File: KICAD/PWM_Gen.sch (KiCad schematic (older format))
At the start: 13 parts, among them U1 AD8030, U2 AD8030

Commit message: review w/ jmt
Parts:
- C26: renamed from C?; footprint Capacitor_SMD:C_0805_2012Metric_Pad1.15x1.40mm_HandSolder -> (none)
- R70, R71, R72, R73, R74, R75: renamed from R?; footprint Resistor_SMD:R_0805_2012Metric_Pad1.15x1.40mm_HandSolder -> (none)
- U1: footprint Package_SO:SO-8_3.9x4.9mm_P1.27mm -> (none)
- U13: renamed from U2; footprint Package_SO:SO-8_3.9x4.9mm_P1.27mm -> (none)
- gave numbers to parts that had none: 4
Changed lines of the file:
@@
 $Descr A4 11693 8268
 encoding utf-8
-Sheet 14 17
+Sheet 13 17
 Title "SESAME"
 Date ""
@@
 AR Path="/60F19D5B/613D641B" Ref="R?"  Part="1"
 AR Path="/60F171CE/613D641B" Ref="R?"  Part="1"
-AR Path="/60F1AF26/613D641B" Ref="R?"  Part="1"
-F 0 "R?" V 5207 3050 50  0000 C CNN
+AR Path="/60F1AF26/613D641B" Ref="R73"  Part="1"
+F 0 "R73" V 5207 3050 50  0000 C CNN
 F 1 "100k" V 5116 3050 50  0000 C CNN
-F 2 "Resistor_SMD:R_0805_2012Metric_Pad1.15x1.40mm_HandSolder" V 4930 3050 50  0001 C CNN
+F 2 "" V 4930 3050 50  0001 C CNN
 F 3 "~" H 5000 3050 50  0001 C CNN
 	1    5000 3050
@@
 AR Path="/60F19D5B/613D6415" Ref="R?"  Part="1"
 AR Path="/60F171CE/613D6415" Ref="R?"  Part="1"
-AR Path="/60F1AF26/613D6415" Ref="R?"  Part="1"
-F 0 "R?" V 5207 2850 50  0000 C CNN
+AR Path="/60F1AF26/613D6415" Ref="R72"  Part="1"
+F 0 "R72" V 5207 2850 50  0000 C CNN
 F 1 "100k" V 5116 2850 50  0000 C CNN
-F 2 "Resistor_SMD:R_0805_2012Metric_Pad1.15x1.40mm_HandSolder" V 4930 2850 50  0001 C CNN
+F 2 "" V 4930 2850 50  0001 C CNN
 F 3 "~" H 5000 2850 50  0001 C CNN
 	1    5000 2850
@@
 AR Path="/60F19D5B/613D6432" Ref="#PWR?"  Part="1"
 AR Path="/60F171CE/613D6432" Ref="#PWR?"  Part="1"
-AR Path="/60F1AF26/613D6432" Ref="#PWR0116"  Part="1"
-F 0 "#PWR0116" H 5350 3300 50  0001 C CNN
+AR Path="/60F1AF26/613D6432" Ref="#PWR090"  Part="1"
+F 0 "#PWR090" H 5350 3300 50  0001 C CNN
 F 1 "GND" H 5355 3377 50  0000 C CNN
 F 2 "" H 5350 3550 50  0001 C CNN
@@
 AR Path="/60F19D5B/613D6429" Ref="R?"  Part="1"
 AR Path="/60F171CE/613D6429" Ref="R?"  Part="1"
-AR Path="/60F1AF26/613D6429" Ref="R?"  Part="1"
-F 0 "R?" H 5420 3446 50  0000 L CNN
+AR Path="/60F1AF26/613D6429" Ref="R74"  Part="1"
+F 0 "R74" H 5420 3446 50  0000 L CNN
 F 1 "100k" H 5420 3355 50  0000 L CNN
-F 2 "Resistor_SMD:R_0805_2012Metric_Pad1.15x1.40mm_HandSolder" V 5280 3400 50  0001 C CNN
+F 2 "" V 5280 3400 50  0001 C CNN
 F 3 "~" H 5350 3400 50  0001 C CNN
 	1    5350 3400
@@
 AR Path="/60F19D5B/613D9855" Ref="R?"  Part="1"
 AR Path="/60F171CE/613D9855" Ref="R?"  Part="1"
-AR Path="/60F1AF26/613D9855" Ref="R?"  Part="1"
-F 0 "R?" H 3070 3096 50  0000 L CNN
+AR Path="/60F1AF26/613D9855" Ref="R71"  Part="1"
+F 0 "R71" H 3070 3096 50  0000 L CNN
 F 1 "4.7k" H 3070 3005 50  0000 L CNN
-F 2 "Resistor_SMD:R_0805_2012Metric_Pad1.15x1.40mm_HandSolder" V 2930 3050 50  0001 C CNN
+F 2 "" V 2930 3050 50  0001 C CNN
 F 3 "~" H 3000 3050 50  0001 C CNN
 	1    3000 3050
@@
 AR Path="/60F19D5B/613D9F4F" Ref="#PWR?"  Part="1"
 AR Path="/60F171CE/613D9F4F" Ref="#PWR?"  Part="1"
-AR Path="/60F1AF26/613D9F4F" Ref="#PWR0117"  Part="1"
-F 0 "#PWR0117" H 3000 2950 50  0001 C CNN
+AR Path="/60F1AF26/613D9F4F" Ref="#PWR089"  Part="1"
+F 0 "#PWR089" H 3000 2950 50  0001 C CNN
 F 1 "GND" H 3005 3027 50  0000 C CNN
 F 2 "" H 3000 3200 50  0001 C CNN
@@
 Same IC package than the Feedback block
 $Comp
-L Sesame:AD8030 U2
+L Sesame:AD8030 U13
 U 1 1 6128401D
 P 8200 3050
-F 0 "U2" H 8200 2683 50  0000 C CNN
+F 0 "U13" H 8200 2683 50  0000 C CNN
 F 1 "AD8030" H 8200 2774 50  0000 C CNN
-F 2 "Package_SO:SO-8_3.9x4.9mm_P1.27mm" H 8200 3050 50  0001 C CNN
+F 2 "" H 8200 3050 50  0001 C CNN
 F 3 "~" H 8200 3050 50  0001 C CNN
 	1    8200 3050
@@
 $EndComp
 $Comp
-L Sesame:AD8030 U2
+L Sesame:AD8030 U13
 U 2 1 61284FE7
 P 8200 3950
-F 0 "U2" H 8200 3583 50  0000 C CNN
+F 0 "U13" H 8200 3583 50  0000 C CNN
 F 1 "AD8030" H 8200 3674 50  0000 C CNN
-F 2 "Package_SO:SO-8_3.9x4.9mm_P1.27mm" H 8200 3950 50  0001 C CNN
+F 2 "" H 8200 3950 50  0001 C CNN
 F 3 "~" H 8200 3950 50  0001 C CNN
 	2    8200 3950
@@
 F 0 "U1" H 5700 3350 50  0000 C CNN
 F 1 "AD8030" H 5700 3250 50  0000 C CNN
-F 2 "Package_SO:SO-8_3.9x4.9mm_P1.27mm" H 5700 2950 50  0001 C CNN
+F 2 "" H 5700 2950 50  0001 C CNN
 F 3 "~" H 5700 2950 50  0001 C CNN
 	2    5700 2950
@@
 $EndComp
 $Comp
-L Sesame:VREF #PWR0120
+L Sesame:VREF #PWR088
 U 1 1 6154E004
 P 3000 2500
-F 0 "#PWR0120" H 3000 2350 50  0001 C CNN
+F 0 "#PWR088" H 3000 2350 50  0001 C CNN
 F 1 "VREF" H 3015 2673 50  0000 C CNN
 F 2 "" H 3000 2500 50  0001 C CNN
@@
 AR Path="/60F19D5B/613D8CB8" Ref="R?"  Part="1"
 AR Path="/60F171CE/613D8CB8" Ref="R?"  Part="1"
-AR Path="/60F1AF26/613D8CB8" Ref="R?"  Part="1"
-F 0 "R?" H 3070 2696 50  0000 L CNN
+AR Path="/60F1AF26/613D8CB8" Ref="R70"  Part="1"
+F 0 "R70" H 3070 2696 50  0000 L CNN
 F 1 "100k" H 3070 2605 50  0000 L CNN
-F 2 "Resistor_SMD:R_0805_2012Metric_Pad1.15x1.40mm_HandSolder" V 2930 2650 50  0001 C CNN
+F 2 "" V 2930 2650 50  0001 C CNN
 F 3 "~" H 3000 2650 50  0001 C CNN
 	1    3000 2650
@@
 $EndComp
 $Comp
-L Connector:TestPoint TP?
+L Connector:TestPoint TP35
 U 1 1 612937F6
 P 3900 2850
-F 0 "TP?" H 3850 3100 50  0000 L CNN
+F 0 "TP35" H 3850 3100 50  0000 L CNN
 F 1 "TP_NOP" H 3900 2750 50  0000 C CNN
 F 2 "" H 4100 2850 50  0001 C CNN
@@
 	3000 2850 3900 2850
 $Comp
-L Connector:TestPoint TP?
+L Connector:TestPoint TP36
 U 1 1 61299A59
 P 6600 2950
-F 0 "TP?" H 6550 3200 50  0000 L CNN
+F 0 "TP36" H 6550 3200 50  0000 L CNN
 F 1 "TP_POP" H 6600 2850 50  0000 C CNN
 F 2 "" H 6800 2950 50  0001 C CNN
@@
 	6600 2950 7900 2950
 $Comp
-L Connector:TestPoint TP?
+L Connector:TestPoint TP38
 U 1 1 612A9FCA
 P 9150 3950
-F 0 "TP?" H 9100 4200 50  0000 L CNN
+F 0 "TP38" H 9100 4200 50  0000 L CNN
 F 1 "TP_POP" H 9150 3850 50  0000 C CNN
 F 2 "" H 9350 3950 50  0001 C CNN
@@
 	9150 3950 8500 3950
 $Comp
-L Connector:TestPoint TP?
+L Connector:TestPoint TP37
 U 1 1 612A923F
 P 9150 3050
-F 0 "TP?" H 9100 3300 50  0000 L CNN
+F 0 "TP37" H 9100 3300 50  0000 L CNN
 F 1 "TP_POP" H 9150 2950 50  0000 C CNN
 F 2 "" H 9350 3050 50  0001 C CNN
@@
 OP Amp supply
 $Comp
-L Device:C C?
+L Device:C C26
 U 1 1 612CB355
 P 1350 6900
-AR Path="/60F1AF26/612CB355" Ref="C?"  Part="1"
+AR Path="/60F1AF26/612CB355" Ref="C26"  Part="1"
 AR Path="/60F1B237/612CB355" Ref="C?"  Part="1"
-F 0 "C?" H 1465 6946 50  0000 L CNN
+F 0 "C26" H 1465 6946 50  0000 L CNN
 F 1 "100n" H 1465 6855 50  0000 L CNN
-F 2 "Capacitor_SMD:C_0805_2012Metric_Pad1.15x1.40mm_HandSolder" H 1388 6750 50  0001 C CNN
+F 2 "" H 1388 6750 50  0001 C CNN
 F 3 "~" H 1350 6900 50  0001 C CNN
 	1    1350 6900
@@
 	1050 7250 1050 7200
 $Comp
-L power:GND #PWR?
+L power:GND #PWR087
 U 1 1 612CB360
 P 1200 7300
-AR Path="/60F1AF26/612CB360" Ref="#PWR?"  Part="1"
+AR Path="/60F1AF26/612CB360" Ref="#PWR087"  Part="1"
 AR Path="/60F1B237/612CB360" Ref="#PWR?"  Part="1"
-F 0 "#PWR?" H 1200 7050 50  0001 C CNN
+F 0 "#PWR087" H 1200 7050 50  0001 C CNN
 F 1 "GND" H 1205 7127 50  0000 C CNN
 F 2 "" H 1200 7300 50  0001 C CNN
@@
 	1200 7250 1350 7250
 $Comp
-L power:VCC #PWR?
+L power:VCC #PWR086
 U 1 1 612CB36D
 P 1200 6500
-AR Path="/60F1AF26/612CB36D" Ref="#PWR?"  Part="1"
+AR Path="/60F1AF26/612CB36D" Ref="#PWR086"  Part="1"
 AR Path="/60F1B237/612CB36D" Ref="#PWR?"  Part="1"
-F 0 "#PWR?" H 1200 6350 50  0001 C CNN
+F 0 "#PWR086" H 1200 6350 50  0001 C CNN
 F 1 "VCC" H 1215 6673 50  0000 C CNN
 F 2 "" H 1200 6500 50  0001 C CNN
@@
 $EndComp
 $Comp
-L Sesame:AD8030 U2
+L Sesame:AD8030 U13
 U 3 1 612CB373
 P 1150 6900
-AR Path="/60F1AF26/612CB373" Ref="U2"  Part="3"
+AR Path="/60F1AF26/612CB373" Ref="U13"  Part="3"
 AR Path="/60F1B237/612CB373" Ref="U?"  Part="3"
-F 0 "U2" H 963 6854 50  0000 R CNN
+F 0 "U13" H 963 6854 50  0000 R CNN
 F 1 "AD8030" H 963 6945 50  0000 R CNN
-F 2 "Package_SO:SO-8_3.9x4.9mm_P1.27mm" H 1150 6900 50  0001 C CNN
+F 2 "" H 1150 6900 50  0001 C CNN
 F 3 "~" H 1150 6900 50  0001 C CNN
 	3    1150 6900
@@
 AR Path="/60F19D5B/613D640F" Ref="R?"  Part="1"
 AR Path="/60F171CE/613D640F" Ref="R?"  Part="1"
-AR Path="/60F1AF26/613D640F" Ref="R?"  Part="1"
-F 0 "R?" V 5907 2600 50  0000 C CNN
+AR Path="/60F1AF26/613D640F" Ref="R75"  Part="1"
+F 0 "R75" V 5907 2600 50  0000 C CNN
 F 1 "100k" V 5816 2600 50  0000 C CNN
-F 2 "Resistor_SMD:R_0805_2012Metric_Pad1.15x1.40mm_HandSolder" V 5630 2600 50  0001 C CNN
+F 2 "" V 5630 2600 50  0001 C CNN
 F 3 "~" H 5700 2600 50  0001 C CNN
 	1    5700 2600

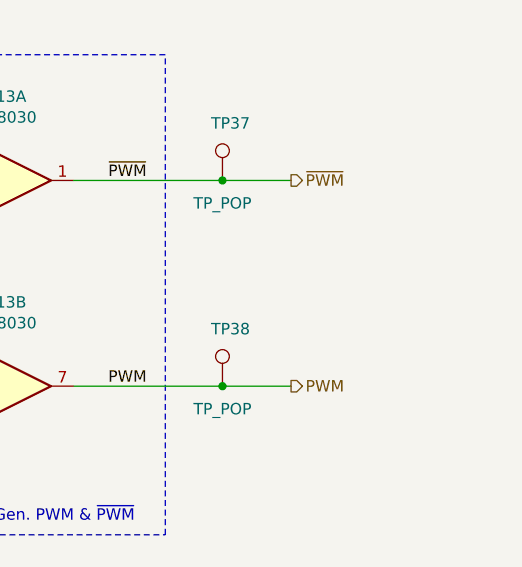
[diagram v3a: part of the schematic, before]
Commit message: edit footprints by jmt
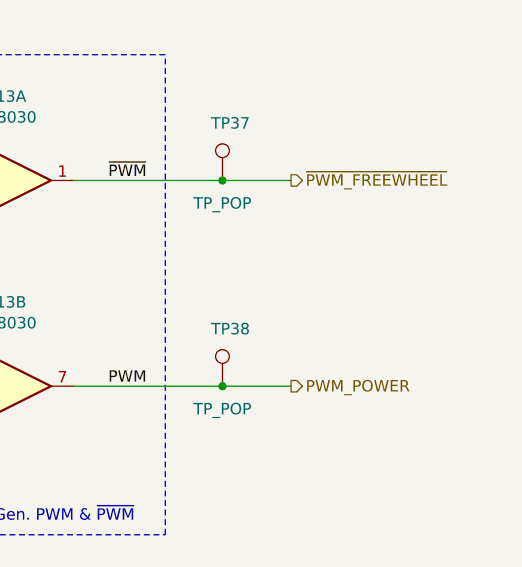
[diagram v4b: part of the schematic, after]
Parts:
- C26: footprint (none) -> Capacitor_SMD:C_0805_2012Metric_Pad1.15x1.40mm_HandSolder
- R70, R71, R72, R73, R74, R75: footprint (none) -> Resistor_SMD:R_0805_2012Metric_Pad1.15x1.40mm_HandSolder
- TP35: footprint (none) -> TestPoint:TestPoint_THTPad_D2.0mm_Drill1.0mm
- TP36, TP37, TP38: footprint (none) -> TestPoint:TestPoint_Loop_D1.80mm_Drill1.0mm_Beaded
- U1, U13: footprint (none) -> Package_SO:SO-8_5.3x6.2mm_P1.27mm
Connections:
- net PWM renamed PWM_POWER
- net ~PWM renamed ~PWM_FREEWHEEL
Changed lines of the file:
@@
 F 0 "R73" V 5207 3050 50  0000 C CNN
 F 1 "100k" V 5116 3050 50  0000 C CNN
-F 2 "" V 4930 3050 50  0001 C CNN
+F 2 "Resistor_SMD:R_0805_2012Metric_Pad1.15x1.40mm_HandSolder" V 4930 3050 50  0001 C CNN
 F 3 "~" H 5000 3050 50  0001 C CNN
 	1    5000 3050
@@
 F 0 "R72" V 5207 2850 50  0000 C CNN
 F 1 "100k" V 5116 2850 50  0000 C CNN
-F 2 "" V 4930 2850 50  0001 C CNN
+F 2 "Resistor_SMD:R_0805_2012Metric_Pad1.15x1.40mm_HandSolder" V 4930 2850 50  0001 C CNN
 F 3 "~" H 5000 2850 50  0001 C CNN
 	1    5000 2850
@@
 F 0 "R74" H 5420 3446 50  0000 L CNN
 F 1 "100k" H 5420 3355 50  0000 L CNN
-F 2 "" V 5280 3400 50  0001 C CNN
+F 2 "Resistor_SMD:R_0805_2012Metric_Pad1.15x1.40mm_HandSolder" V 5280 3400 50  0001 C CNN
 F 3 "~" H 5350 3400 50  0001 C CNN
 	1    5350 3400
@@
 F 0 "R71" H 3070 3096 50  0000 L CNN
 F 1 "4.7k" H 3070 3005 50  0000 L CNN
-F 2 "" V 2930 3050 50  0001 C CNN
+F 2 "Resistor_SMD:R_0805_2012Metric_Pad1.15x1.40mm_HandSolder" V 2930 3050 50  0001 C CNN
 F 3 "~" H 3000 3050 50  0001 C CNN
 	1    3000 3050
@@
 	8500 3050 9150 3050
 Text HLabel 9450 3050 2    50   Output ~ 0
-~PWM
+~PWM_FREEWHEEL
 Text HLabel 9450 3950 2    50   Output ~ 0
-PWM
+PWM_POWER
 Text HLabel 6850 3500 0    50   Input ~ 0
 Ramp
@@
 F 0 "U13" H 8200 2683 50  0000 C CNN
 F 1 "AD8030" H 8200 2774 50  0000 C CNN
-F 2 "" H 8200 3050 50  0001 C CNN
+F 2 "Package_SO:SO-8_5.3x6.2mm_P1.27mm" H 8200 3050 50  0001 C CNN
 F 3 "~" H 8200 3050 50  0001 C CNN
 	1    8200 3050
@@
 F 0 "U13" H 8200 3583 50  0000 C CNN
 F 1 "AD8030" H 8200 3674 50  0000 C CNN
-F 2 "" H 8200 3950 50  0001 C CNN
+F 2 "Package_SO:SO-8_5.3x6.2mm_P1.27mm" H 8200 3950 50  0001 C CNN
 F 3 "~" H 8200 3950 50  0001 C CNN
 	2    8200 3950
@@
 F 0 "U1" H 5700 3350 50  0000 C CNN
 F 1 "AD8030" H 5700 3250 50  0000 C CNN
-F 2 "" H 5700 2950 50  0001 C CNN
+F 2 "Package_SO:SO-8_5.3x6.2mm_P1.27mm" H 5700 2950 50  0001 C CNN
 F 3 "~" H 5700 2950 50  0001 C CNN
 	2    5700 2950
@@
 F 0 "R70" H 3070 2696 50  0000 L CNN
 F 1 "100k" H 3070 2605 50  0000 L CNN
-F 2 "" V 2930 2650 50  0001 C CNN
+F 2 "Resistor_SMD:R_0805_2012Metric_Pad1.15x1.40mm_HandSolder" V 2930 2650 50  0001 C CNN
 F 3 "~" H 3000 2650 50  0001 C CNN
 	1    3000 2650
@@
 F 0 "TP35" H 3850 3100 50  0000 L CNN
 F 1 "TP_NOP" H 3900 2750 50  0000 C CNN
-F 2 "" H 4100 2850 50  0001 C CNN
+F 2 "TestPoint:TestPoint_THTPad_D2.0mm_Drill1.0mm" H 4100 2850 50  0001 C CNN
 F 3 "~" H 4100 2850 50  0001 C CNN
 	1    3900 2850
@@
 F 0 "TP36" H 6550 3200 50  0000 L CNN
 F 1 "TP_POP" H 6600 2850 50  0000 C CNN
-F 2 "" H 6800 2950 50  0001 C CNN
+F 2 "TestPoint:TestPoint_Loop_D1.80mm_Drill1.0mm_Beaded" H 6800 2950 50  0001 C CNN
 F 3 "~" H 6800 2950 50  0001 C CNN
 	1    6600 2950
@@
 F 0 "TP38" H 9100 4200 50  0000 L CNN
 F 1 "TP_POP" H 9150 3850 50  0000 C CNN
-F 2 "" H 9350 3950 50  0001 C CNN
+F 2 "TestPoint:TestPoint_Loop_D1.80mm_Drill1.0mm_Beaded" H 9350 3950 50  0001 C CNN
 F 3 "~" H 9350 3950 50  0001 C CNN
 	1    9150 3950
@@
 F 0 "TP37" H 9100 3300 50  0000 L CNN
 F 1 "TP_POP" H 9150 2950 50  0000 C CNN
-F 2 "" H 9350 3050 50  0001 C CNN
+F 2 "TestPoint:TestPoint_Loop_D1.80mm_Drill1.0mm_Beaded" H 9350 3050 50  0001 C CNN
 F 3 "~" H 9350 3050 50  0001 C CNN
 	1    9150 3050
@@
 F 0 "C26" H 1465 6946 50  0000 L CNN
 F 1 "100n" H 1465 6855 50  0000 L CNN
-F 2 "" H 1388 6750 50  0001 C CNN
+F 2 "Capacitor_SMD:C_0805_2012Metric_Pad1.15x1.40mm_HandSolder" H 1388 6750 50  0001 C CNN
 F 3 "~" H 1350 6900 50  0001 C CNN
 	1    1350 6900
@@
 F 0 "U13" H 963 6854 50  0000 R CNN
 F 1 "AD8030" H 963 6945 50  0000 R CNN
-F 2 "" H 1150 6900 50  0001 C CNN
+F 2 "Package_SO:SO-8_5.3x6.2mm_P1.27mm" H 1150 6900 50  0001 C CNN
 F 3 "~" H 1150 6900 50  0001 C CNN
 	3    1150 6900
@@
 F 0 "R75" V 5907 2600 50  0000 C CNN
 F 1 "100k" V 5816 2600 50  0000 C CNN
-F 2 "" V 5630 2600 50  0001 C CNN
+F 2 "Resistor_SMD:R_0805_2012Metric_Pad1.15x1.40mm_HandSolder" V 5630 2600 50  0001 C CNN
 F 3 "~" H 5700 2600 50  0001 C CNN
 	1    5700 2600

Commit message: route + work on djd
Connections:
- net PWM_POWER renamed PWM_Power
- net ~PWM_FREEWHEEL renamed ~PWM_Freewheel
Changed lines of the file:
@@
 $Descr A4 11693 8268
 encoding utf-8
-Sheet 13 17
+Sheet 17 17
 Title "SESAME"
 Date ""
@@
 	8500 3050 9150 3050
 Text HLabel 9450 3050 2    50   Output ~ 0
-~PWM_FREEWHEEL
+~PWM_Freewheel
 Text HLabel 9450 3950 2    50   Output ~ 0
-PWM_POWER
+PWM_Power
 Text HLabel 6850 3500 0    50   Input ~ 0
 Ramp
@@
 	1    0    0    -1
 $EndComp
-Connection ~ 9150 3050
-Wire Wire Line
-	9150 3050 9450 3050
 Connection ~ 9150 3950
 Wire Wire Line
@@
 	0    -1   -1   0
 $EndComp
+Connection ~ 9150 3050
+Wire Wire Line
+	9150 3050 9450 3050
 $EndSCHEMATC

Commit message: added footprint for sepic coil + no more errors in netlist
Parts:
- C26: footprint Capacitor_SMD:C_0805_2012Metric_Pad1.15x1.40mm_HandSolder -> Sesame_footprint:C_0805_2012Metric_Pad1.18x1.45mm_HandSolder
- R70, R71, R72, R73, R74, R75: footprint Resistor_SMD:R_0805_2012Metric_Pad1.15x1.40mm_HandSolder -> Sesame_footprint:R_0805_2012Metric_Pad1.20x1.40mm_HandSolder
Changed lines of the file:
@@
 F 0 "R73" V 5207 3050 50  0000 C CNN
 F 1 "100k" V 5116 3050 50  0000 C CNN
-F 2 "Resistor_SMD:R_0805_2012Metric_Pad1.15x1.40mm_HandSolder" V 4930 3050 50  0001 C CNN
+F 2 "Sesame_footprint:R_0805_2012Metric_Pad1.20x1.40mm_HandSolder" V 4930 3050 50  0001 C CNN
 F 3 "~" H 5000 3050 50  0001 C CNN
 	1    5000 3050
@@
 F 0 "R72" V 5207 2850 50  0000 C CNN
 F 1 "100k" V 5116 2850 50  0000 C CNN
-F 2 "Resistor_SMD:R_0805_2012Metric_Pad1.15x1.40mm_HandSolder" V 4930 2850 50  0001 C CNN
+F 2 "Sesame_footprint:R_0805_2012Metric_Pad1.20x1.40mm_HandSolder" V 4930 2850 50  0001 C CNN
 F 3 "~" H 5000 2850 50  0001 C CNN
 	1    5000 2850
@@
 F 0 "R74" H 5420 3446 50  0000 L CNN
 F 1 "100k" H 5420 3355 50  0000 L CNN
-F 2 "Resistor_SMD:R_0805_2012Metric_Pad1.15x1.40mm_HandSolder" V 5280 3400 50  0001 C CNN
+F 2 "Sesame_footprint:R_0805_2012Metric_Pad1.20x1.40mm_HandSolder" V 5280 3400 50  0001 C CNN
 F 3 "~" H 5350 3400 50  0001 C CNN
 	1    5350 3400
@@
 F 0 "R71" H 3070 3096 50  0000 L CNN
 F 1 "4.7k" H 3070 3005 50  0000 L CNN
-F 2 "Resistor_SMD:R_0805_2012Metric_Pad1.15x1.40mm_HandSolder" V 2930 3050 50  0001 C CNN
+F 2 "Sesame_footprint:R_0805_2012Metric_Pad1.20x1.40mm_HandSolder" V 2930 3050 50  0001 C CNN
 F 3 "~" H 3000 3050 50  0001 C CNN
 	1    3000 3050
@@
 F 0 "R70" H 3070 2696 50  0000 L CNN
 F 1 "100k" H 3070 2605 50  0000 L CNN
-F 2 "Resistor_SMD:R_0805_2012Metric_Pad1.15x1.40mm_HandSolder" V 2930 2650 50  0001 C CNN
+F 2 "Sesame_footprint:R_0805_2012Metric_Pad1.20x1.40mm_HandSolder" V 2930 2650 50  0001 C CNN
 F 3 "~" H 3000 2650 50  0001 C CNN
 	1    3000 2650
@@
 F 0 "C26" H 1465 6946 50  0000 L CNN
 F 1 "100n" H 1465 6855 50  0000 L CNN
-F 2 "Capacitor_SMD:C_0805_2012Metric_Pad1.15x1.40mm_HandSolder" H 1388 6750 50  0001 C CNN
+F 2 "Sesame_footprint:C_0805_2012Metric_Pad1.18x1.45mm_HandSolder" H 1388 6750 50  0001 C CNN
 F 3 "~" H 1350 6900 50  0001 C CNN
 	1    1350 6900
@@
 F 0 "R75" V 5907 2600 50  0000 C CNN
 F 1 "100k" V 5816 2600 50  0000 C CNN
-F 2 "Resistor_SMD:R_0805_2012Metric_Pad1.15x1.40mm_HandSolder" V 5630 2600 50  0001 C CNN
+F 2 "Sesame_footprint:R_0805_2012Metric_Pad1.20x1.40mm_HandSolder" V 5630 2600 50  0001 C CNN
 F 3 "~" H 5700 2600 50  0001 C CNN
 	1    5700 2600
